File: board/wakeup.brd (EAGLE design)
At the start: 65 x 56 mm, 41 parts, among them IC2 ATMEGA48/88/168-AU, K1 PIN20X2, Q5 BC846BSMD, Q6 BC846BSMD, Q7 BC846BSMD, Q8 BC846BSMD, U1 EEPROM24

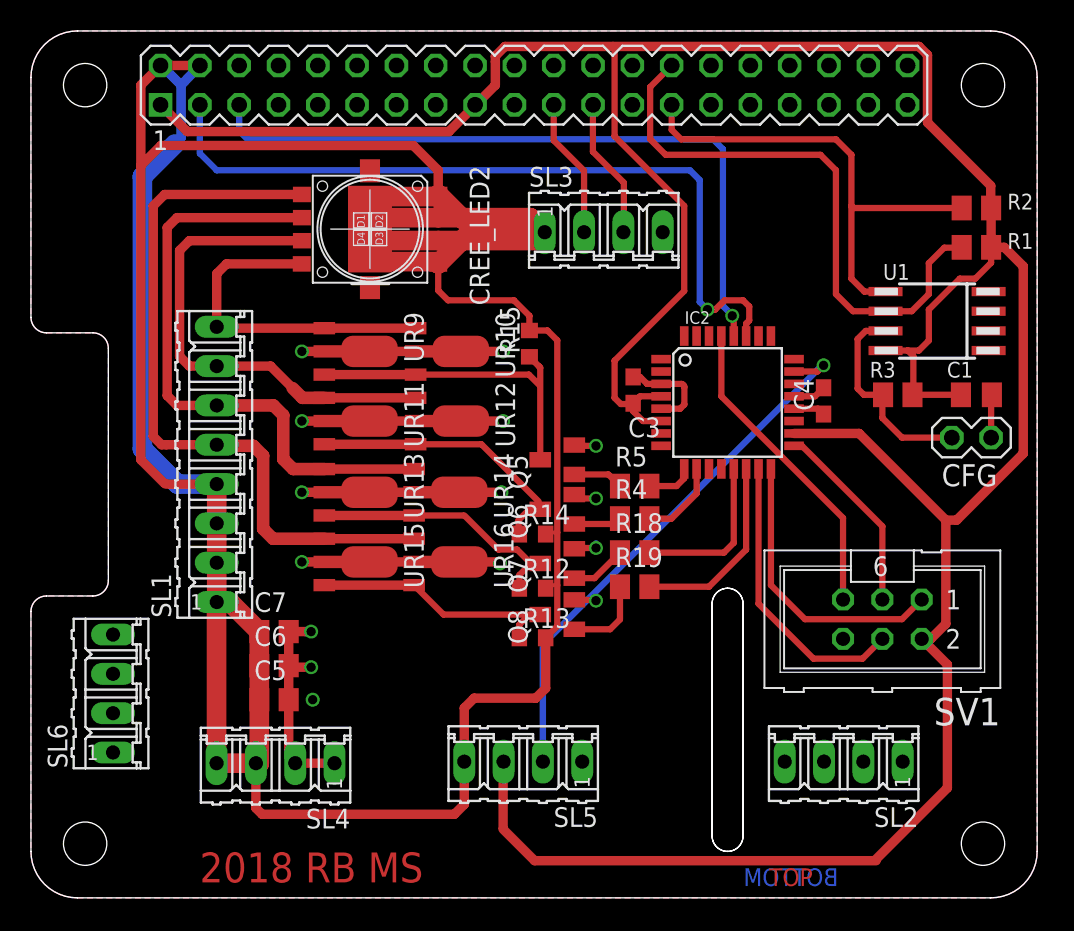
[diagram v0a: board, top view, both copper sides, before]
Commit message: Finalized board. Readded CON_JACK
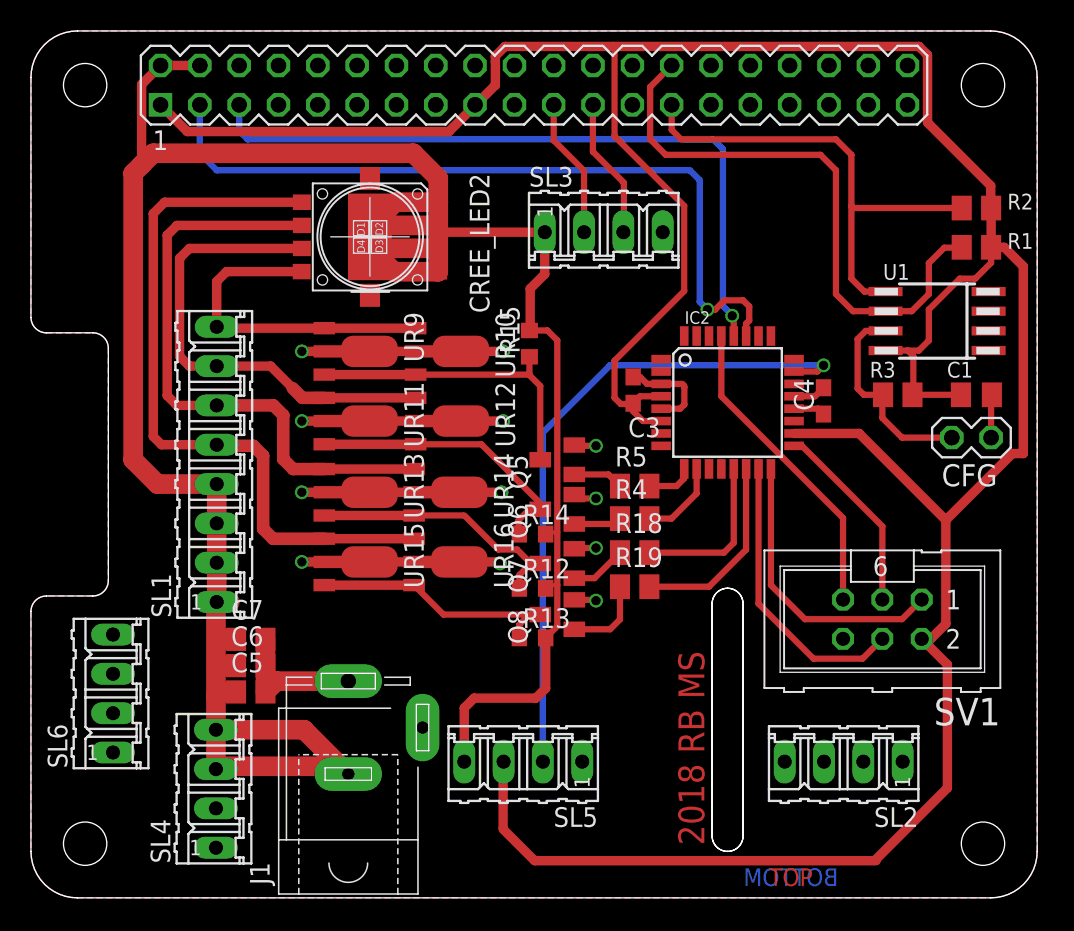
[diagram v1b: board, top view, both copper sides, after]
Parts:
- added J1: (no value), con-jack:SPC4078
- moved SL4 4.19 mm to (11.9, 7.05), turned to 90 degrees
- moved C5 1.58 mm to (14.2, 13.3)
- moved C7 1.58 mm to (14.2, 16.7)
- moved C6 1.50 mm to (14.2, 15.0)
- moved CREE_LED2 0.50 mm to (21.9, 42.7)
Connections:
- net +5V: now also J1.1
- net GND: now also J1.2, J1.3
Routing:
- net +5V: track 231.3 -> 171.1 mm
- net ADC0: track 35.2 -> 43.3 mm
- net GND: track 75.9 -> 69.9 mm, vias 15 -> 12
- net RED_POWER: track 21.1 -> 20.2 mm
- net WHITE_LED_OUT: track 47.2 -> 46.7 mm
- net RED_LED_OUT: track 22.1 -> 21.6 mm
- net GREEN_LED_OUT: track 31.4 -> 30.9 mm
- net BLUE_LED_OUT: track 39.4 -> 38.9 mm
